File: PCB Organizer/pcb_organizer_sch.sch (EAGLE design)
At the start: 2 parts, among them U1 ARDUINO_NANO

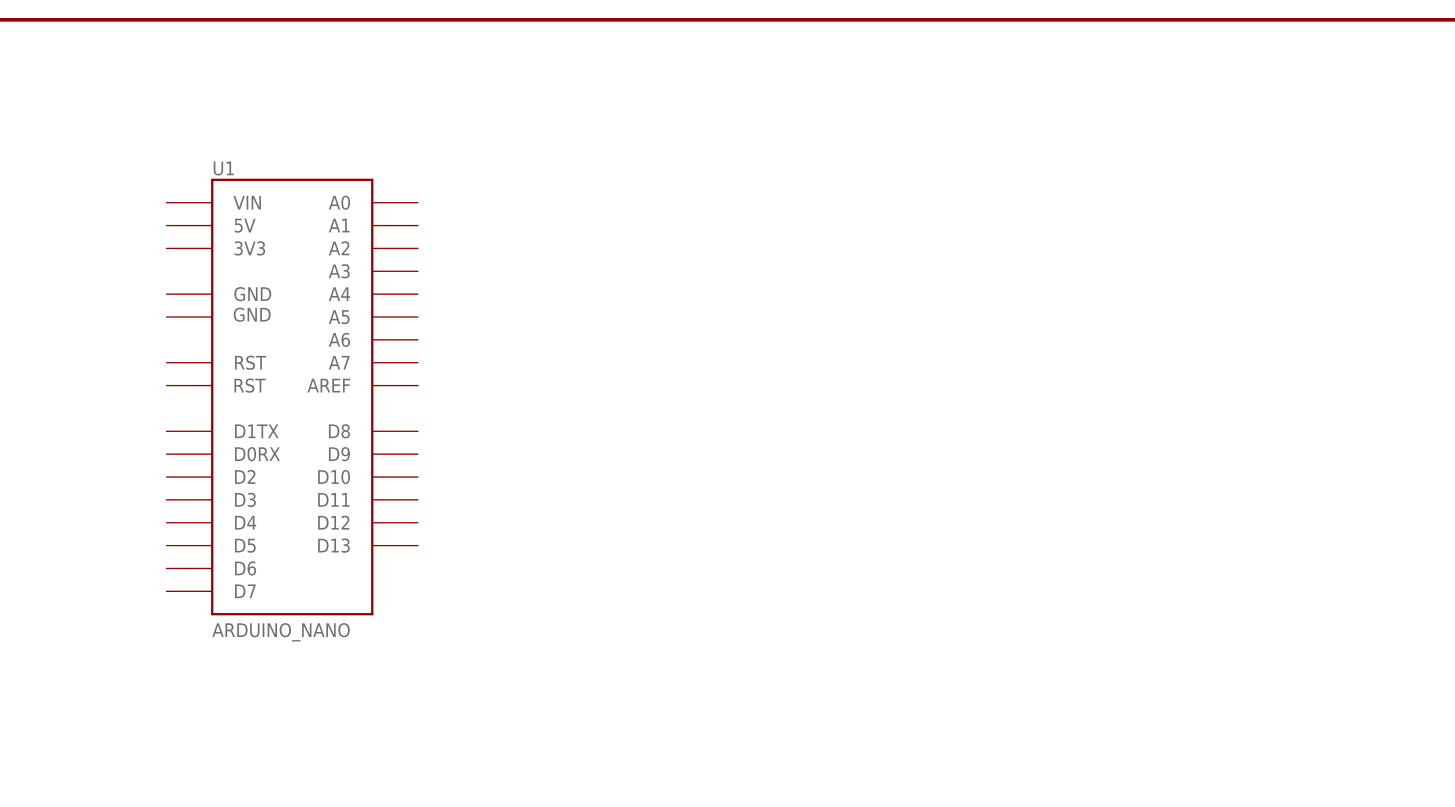
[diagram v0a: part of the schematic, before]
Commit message: Added footprint for V8FR-II receiver
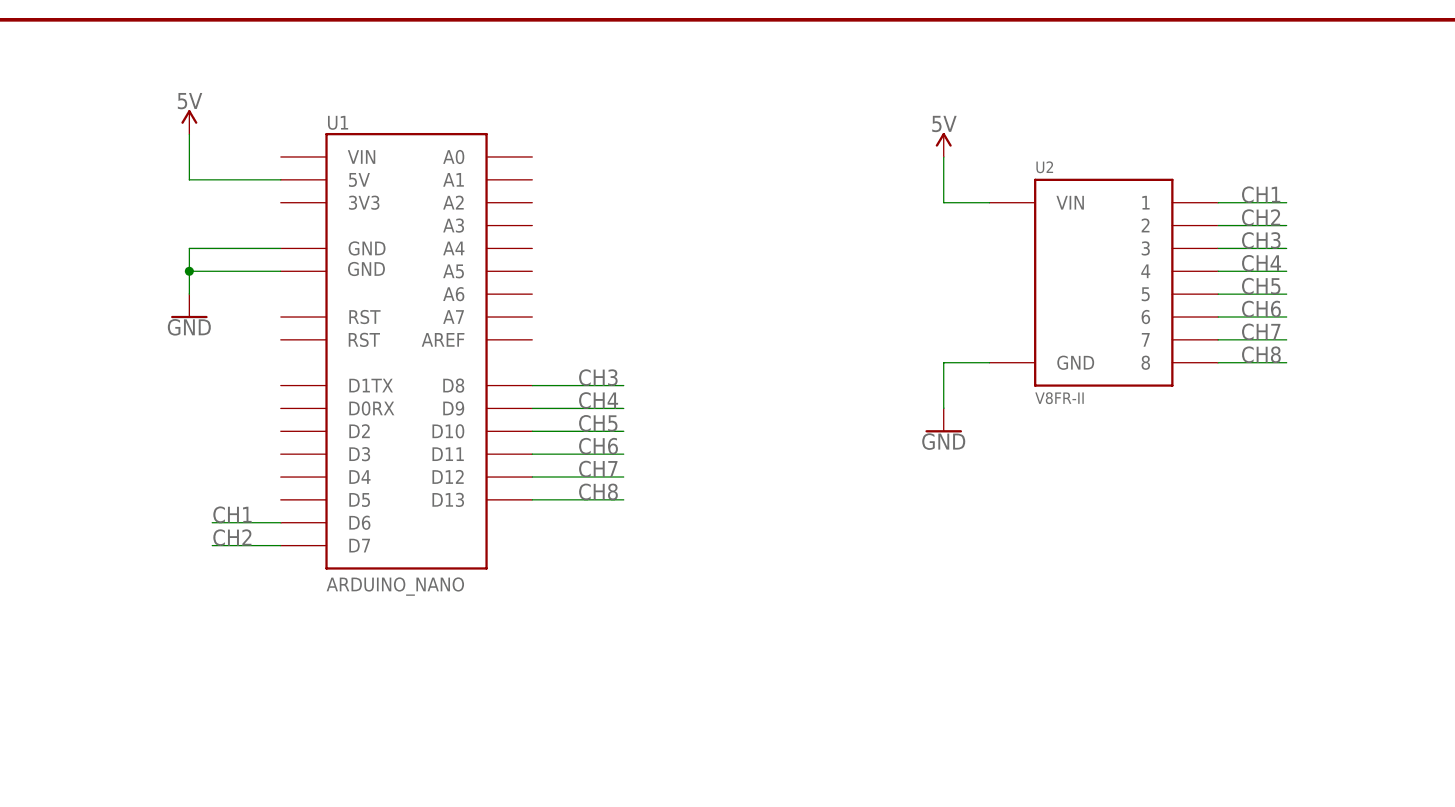
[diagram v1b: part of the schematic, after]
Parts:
- added U2: V8FR-II, CUCombatBots:V8FR-II
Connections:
- new net 5V: U1.5V, U2.VIN
- new net CH1: U1.D6, U2.1
- new net CH2: U1.D7, U2.2
- new net CH3: U1.D8, U2.3
- new net CH4: U1.D9, U2.4
- new net CH5: U1.D10, U2.5
- new net CH6: U1.D11, U2.6
- new net CH7: U1.D12, U2.7
- new net CH8: U1.D13, U2.8
- new net GND: U1.GND, U1.GND@16, U2.GND
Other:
- moved on the sheet: U1
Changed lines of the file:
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@@
 <part name="FRAME1" library="SparkFun-Aesthetics" deviceset="FRAME-LEDGER" device=""/>
 <part name="U1" library="CUCombatBots" deviceset="ARDUINO_NANO" device=""/>
+<part name="U2" library="CUCombatBots" deviceset="V8FR-II" device=""/>
+<part name="GND1" library="SparkFun-PowerSymbols" deviceset="GND" device=""/>
+<part name="GND2" library="SparkFun-PowerSymbols" deviceset="GND" device=""/>
+<part name="SUPPLY1" library="SparkFun-PowerSymbols" deviceset="5V" device=""/>
+<part name="SUPPLY2" library="SparkFun-PowerSymbols" deviceset="5V" device=""/>
 </parts>
 <sheets>
@@
 <attribute name="REV" x="419.1" y="6.604" size="2.7432" layer="94" font="vector"/>
 </instance>
-<instance part="U1" gate="G$1" x="60.96" y="246.38" smashed="yes">
-<attribute name="NAME" x="50.8" y="262.128" size="1.524" layer="95"/>
-<attribute name="VALUE" x="50.8" y="210.82" size="1.524" layer="96"/>
+<instance part="U1" gate="G$1" x="73.66" y="251.46" smashed="yes">
+<attribute name="NAME" x="63.5" y="267.208" size="1.524" layer="95"/>
+<attribute name="VALUE" x="63.5" y="215.9" size="1.524" layer="96"/>
+</instance>
+<instance part="U2" gate="G$1" x="149.86" y="251.46" smashed="yes">
+<attribute name="NAME" x="142.24" y="262.382" size="1.27" layer="95"/>
+<attribute name="VALUE" x="142.24" y="236.728" size="1.27" layer="96"/>
+</instance>
+<instance part="GND1" gate="1" x="132.08" y="233.68" smashed="yes">
+<attribute name="VALUE" x="132.08" y="233.426" size="1.778" layer="96" align="top-center"/>
+</instance>
+<instance part="GND2" gate="1" x="48.26" y="246.38" smashed="yes">
+<attribute name="VALUE" x="48.26" y="246.126" size="1.778" layer="96" align="top-center"/>
+</instance>
+<instance part="SUPPLY1" gate="G$1" x="48.26" y="266.7" smashed="yes">
+<attribute name="VALUE" x="48.26" y="269.494" size="1.778" layer="96" align="bottom-center"/>
+</instance>
+<instance part="SUPPLY2" gate="G$1" x="132.08" y="264.16" smashed="yes">
+<attribute name="VALUE" x="132.08" y="266.954" size="1.778" layer="96" align="bottom-center"/>
 </instance>
 </instances>
@@
 </busses>
 <nets>
+<net name="5V" class="0">
+<segment>
+<pinref part="U2" gate="G$1" pin="VIN"/>
+<wire x1="137.16" y1="259.08" x2="132.08" y2="259.08" width="0.1524" layer="91"/>
+<pinref part="SUPPLY2" gate="G$1" pin="5V"/>
+<wire x1="132.08" y1="259.08" x2="132.08" y2="264.16" width="0.1524" layer="91"/>
+</segment>
+<segment>
+<pinref part="U1" gate="G$1" pin="5V"/>
+<wire x1="58.42" y1="261.62" x2="48.26" y2="261.62" width="0.1524" layer="91"/>
+<pinref part="SUPPLY1" gate="G$1" pin="5V"/>
+<wire x1="48.26" y1="261.62" x2="48.26" y2="266.7" width="0.1524" layer="91"/>
+</segment>
+</net>
+<net name="CH1" class="0">
+<segment>
+<pinref part="U2" gate="G$1" pin="1"/>
+<wire x1="162.56" y1="259.08" x2="170.18" y2="259.08" width="0.1524" layer="91"/>
+<label x="165.1" y="259.08" size="1.778" layer="95"/>
+</segment>
+<segment>
+<pinref part="U1" gate="G$1" pin="D6"/>
+<wire x1="58.42" y1="223.52" x2="50.8" y2="223.52" width="0.1524" layer="91"/>
+<label x="50.8" y="223.52" size="1.778" layer="95"/>
+</segment>
+</net>
+<net name="CH2" class="0">
+<segment>
+<pinref part="U2" gate="G$1" pin="2"/>
+<wire x1="162.56" y1="256.54" x2="170.18" y2="256.54" width="0.1524" layer="91"/>
+<label x="165.1" y="256.54" size="1.778" layer="95"/>
+</segment>
+<segment>
+<pinref part="U1" gate="G$1" pin="D7"/>
+<wire x1="58.42" y1="220.98" x2="50.8" y2="220.98" width="0.1524" layer="91"/>
+<label x="50.8" y="220.98" size="1.778" layer="95"/>
+</segment>
+</net>
+<net name="CH3" class="0">
+<segment>
+<pinref part="U2" gate="G$1" pin="3"/>
+<wire x1="162.56" y1="254" x2="170.18" y2="254" width="0.1524" layer="91"/>
+<label x="165.1" y="254" size="1.778" layer="95"/>
+</segment>
+<segment>
+<pinref part="U1" gate="G$1" pin="D8"/>
+<wire x1="86.36" y1="238.76" x2="96.52" y2="238.76" width="0.1524" layer="91"/>
+<label x="91.44" y="238.76" size="1.778" layer="95"/>
+</segment>
+</net>
+<net name="CH4" class="0">
+<segment>
+<pinref part="U2" gate="G$1" pin="4"/>
+<wire x1="162.56" y1="251.46" x2="170.18" y2="251.46" width="0.1524" layer="91"/>
+<label x="165.1" y="251.46" size="1.778" layer="95"/>
+</segment>
+<segment>
+<pinref part="U1" gate="G$1" pin="D9"/>
+<wire x1="86.36" y1="236.22" x2="96.52" y2="236.22" width="0.1524" layer="91"/>
+<label x="91.44" y="236.22" size="1.778" layer="95"/>
+</segment>
+</net>
+<net name="CH5" class="0">
+<segment>
+<pinref part="U2" gate="G$1" pin="5"/>
+<wire x1="162.56" y1="248.92" x2="170.18" y2="248.92" width="0.1524" layer="91"/>
+<label x="165.1" y="248.92" size="1.778" layer="95"/>
+</segment>
+<segment>
+<pinref part="U1" gate="G$1" pin="D10"/>
+<wire x1="86.36" y1="233.68" x2="96.52" y2="233.68" width="0.1524" layer="91"/>
+<label x="91.44" y="233.68" size="1.778" layer="95"/>
+</segment>
+</net>
+<net name="CH6" class="0">
+<segment>
+<pinref part="U2" gate="G$1" pin="6"/>
+<wire x1="162.56" y1="246.38" x2="170.18" y2="246.38" width="0.1524" layer="91"/>
+<label x="165.1" y="246.38" size="1.778" layer="95"/>
+</segment>
+<segment>
+<pinref part="U1" gate="G$1" pin="D11"/>
+<wire x1="86.36" y1="231.14" x2="96.52" y2="231.14" width="0.1524" layer="91"/>
+<label x="91.44" y="231.14" size="1.778" layer="95"/>
+</segment>
+</net>
+<net name="CH7" class="0">
+<segment>
+<pinref part="U2" gate="G$1" pin="7"/>
+<wire x1="162.56" y1="243.84" x2="170.18" y2="243.84" width="0.1524" layer="91"/>
+<label x="165.1" y="243.84" size="1.778" layer="95"/>
+</segment>
+<segment>
+<pinref part="U1" gate="G$1" pin="D12"/>
+<wire x1="86.36" y1="228.6" x2="96.52" y2="228.6" width="0.1524" layer="91"/>
+<label x="91.44" y="228.6" size="1.778" layer="95"/>
+</segment>
+</net>
+<net name="CH8" class="0">
+<segment>
+<pinref part="U2" gate="G$1" pin="8"/>
+<wire x1="162.56" y1="241.3" x2="170.18" y2="241.3" width="0.1524" layer="91"/>
+<label x="165.1" y="241.3" size="1.778" layer="95"/>
+</segment>
+<segment>
+<pinref part="U1" gate="G$1" pin="D13"/>
+<wire x1="86.36" y1="226.06" x2="96.52" y2="226.06" width="0.1524" layer="91"/>
+<label x="91.44" y="226.06" size="1.778" layer="95"/>
+</segment>
+</net>
+<net name="GND" class="0">
+<segment>
+<pinref part="U2" gate="G$1" pin="GND"/>
+<wire x1="137.16" y1="241.3" x2="132.08" y2="241.3" width="0.1524" layer="91"/>
+<pinref part="GND1" gate="1" pin="GND"/>
+<wire x1="132.08" y1="236.22" x2="132.08" y2="241.3" width="0.1524" layer="91"/>
+</segment>
+<segment>
+<pinref part="U1" gate="G$1" pin="GND"/>
+<wire x1="58.42" y1="254" x2="48.26" y2="254" width="0.1524" layer="91"/>
+<wire x1="48.26" y1="254" x2="48.26" y2="251.46" width="0.1524" layer="91"/>
+<pinref part="U1" gate="G$1" pin="GND@16"/>
+<wire x1="48.26" y1="251.46" x2="58.42" y2="251.46" width="0.1524" layer="91"/>
+<wire x1="48.26" y1="251.46" x2="48.26" y2="248.92" width="0.1524" layer="91"/>
+<junction x="48.26" y="251.46"/>
+<pinref part="GND2" gate="1" pin="GND"/>
+</segment>
+</net>
 </nets>
 </sheet>

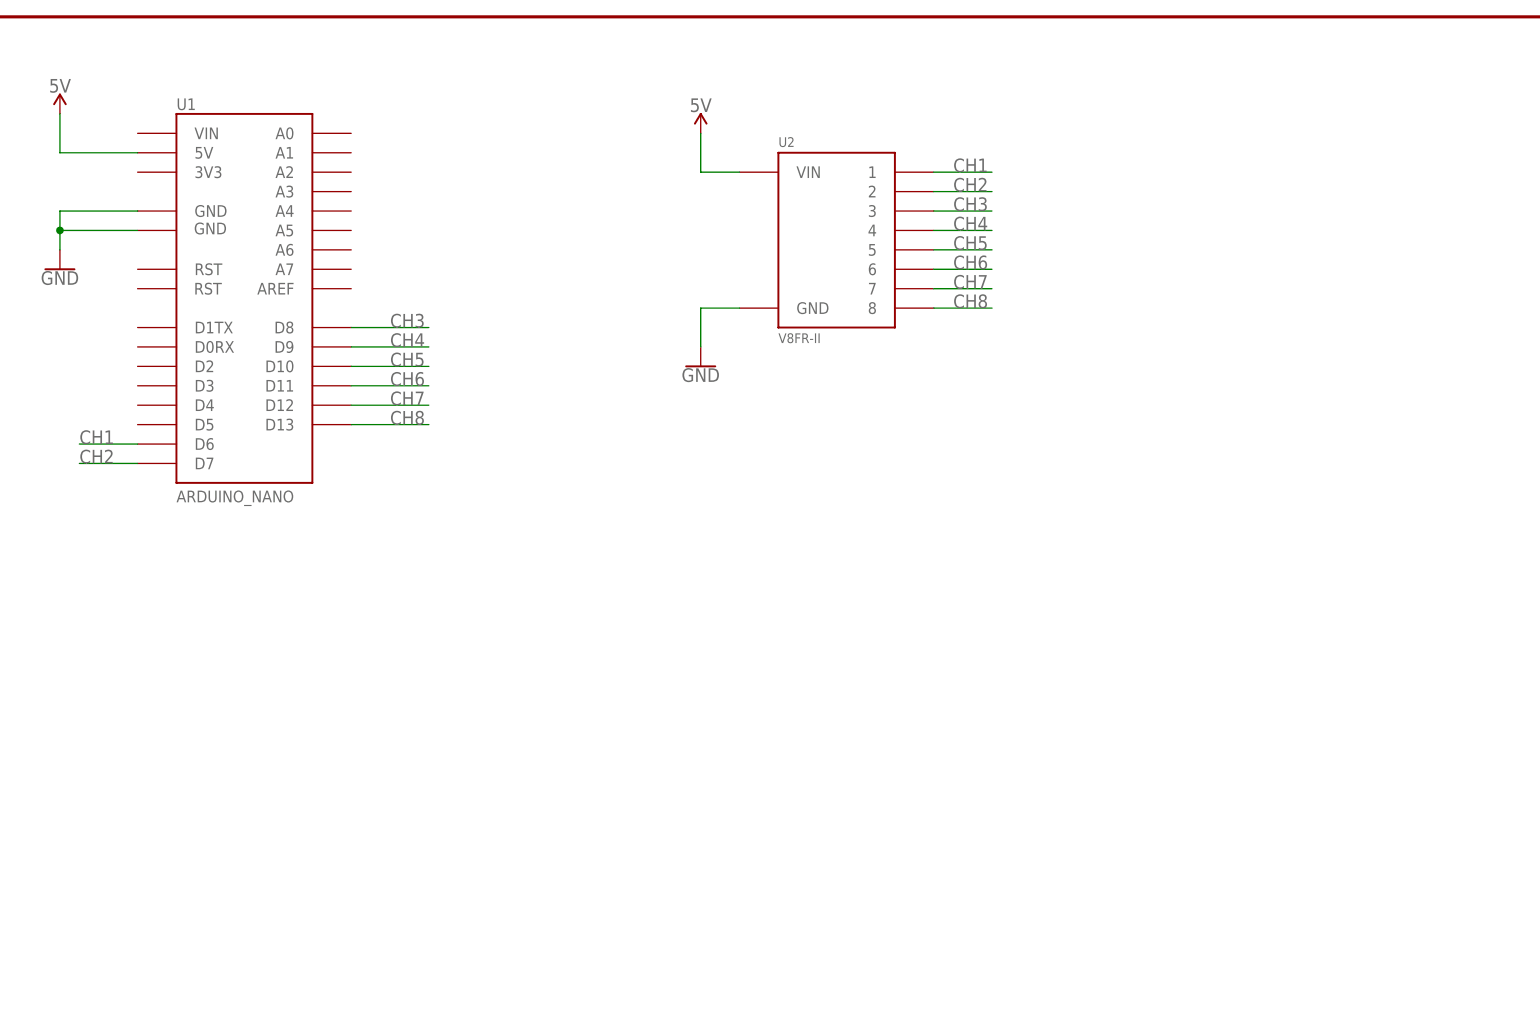
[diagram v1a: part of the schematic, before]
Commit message: Added Pololu TB67 motor driver to the library, board, and schematic
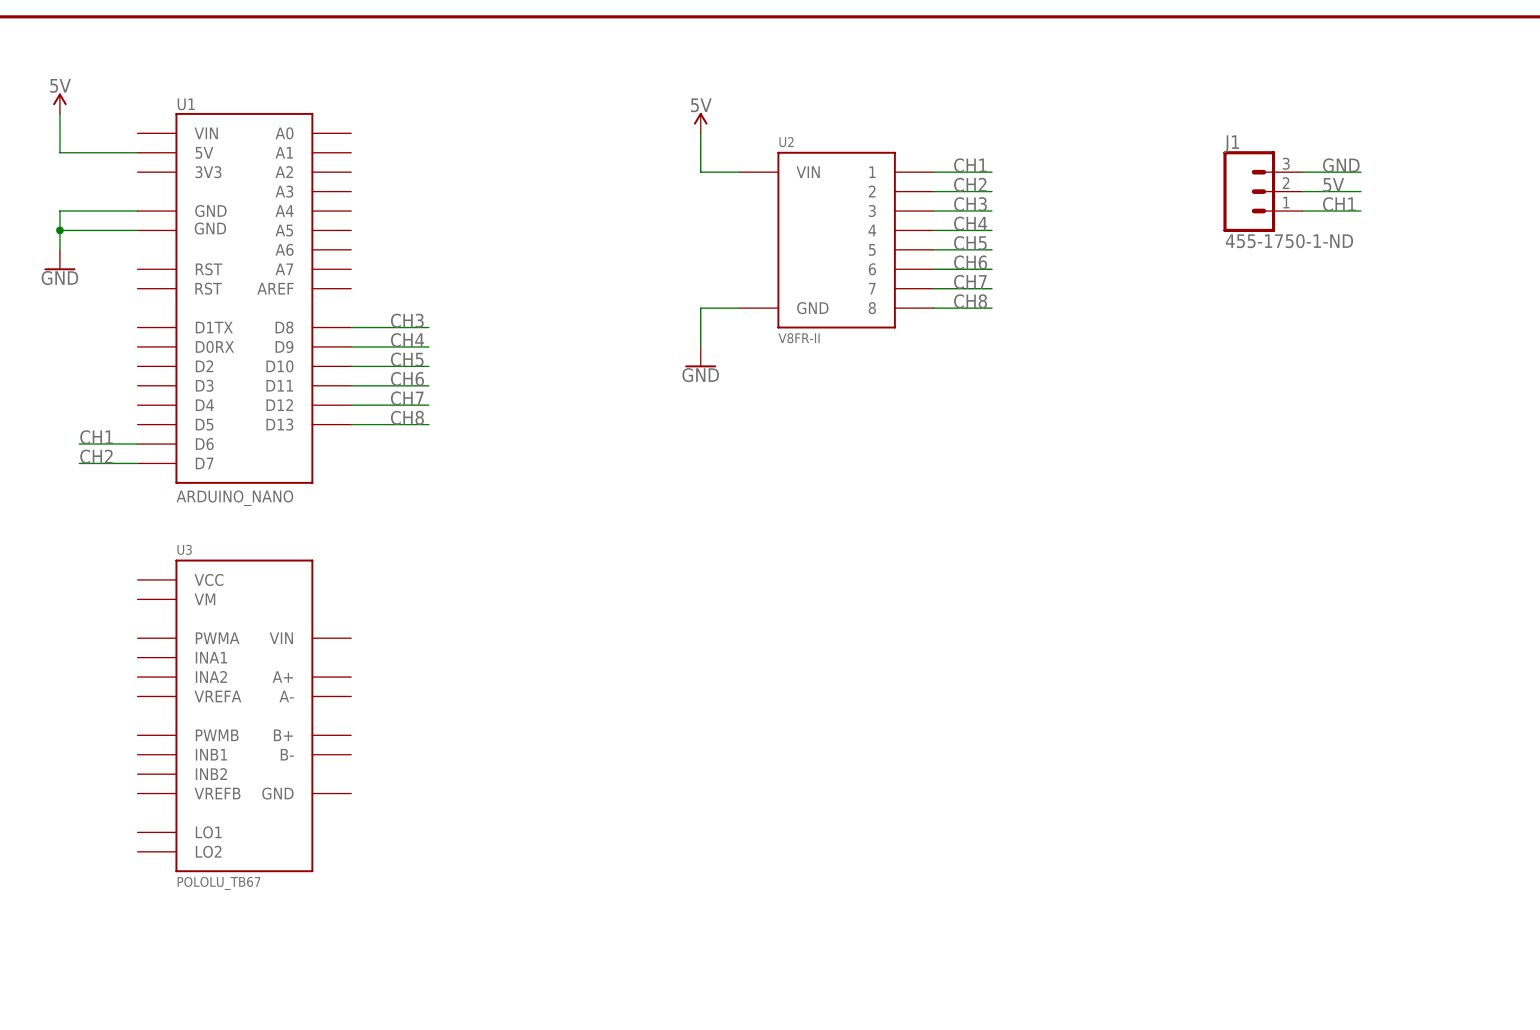
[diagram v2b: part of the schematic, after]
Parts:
- added J1: 455-1750-1-ND, SparkFun-Connectors:CONN_03
- added U3: POLOLU_TB67, CUCombatBots:POLOLU_TB67
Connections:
- net 5V: now also J1.2
- net CH1: now also J1.1
- net GND: now also J1.3
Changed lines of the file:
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@@
 <part name="SUPPLY1" library="SparkFun-PowerSymbols" deviceset="5V" device=""/>
 <part name="SUPPLY2" library="SparkFun-PowerSymbols" deviceset="5V" device=""/>
+<part name="J1" library="SparkFun-Connectors" deviceset="CONN_03" device="" value="455-1750-1-ND"/>
+<part name="U3" library="CUCombatBots" deviceset="POLOLU_TB67" device=""/>
 </parts>
 <sheets>
@@
 <attribute name="VALUE" x="132.08" y="266.954" size="1.778" layer="96" align="bottom-center"/>
 </instance>
+<instance part="J1" gate="J$1" x="203.2" y="256.54" smashed="yes">
+<attribute name="VALUE" x="200.66" y="249.174" size="1.778" layer="96" font="vector"/>
+<attribute name="NAME" x="200.66" y="262.128" size="1.778" layer="95" font="vector"/>
+</instance>
+<instance part="U3" gate="G$1" x="73.66" y="193.04" smashed="yes">
+<attribute name="NAME" x="63.5" y="209.042" size="1.27" layer="95"/>
+<attribute name="VALUE" x="63.5" y="165.608" size="1.27" layer="96"/>
+</instance>
 </instances>
 <busses>
@@
 <wire x1="48.26" y1="261.62" x2="48.26" y2="266.7" width="0.1524" layer="91"/>
 </segment>
+<segment>
+<pinref part="J1" gate="J$1" pin="2"/>
+<wire x1="210.82" y1="256.54" x2="218.44" y2="256.54" width="0.1524" layer="91"/>
+<label x="213.36" y="256.54" size="1.778" layer="95"/>
+</segment>
 </net>
 <net name="CH1" class="0">
@@
 <wire x1="58.42" y1="223.52" x2="50.8" y2="223.52" width="0.1524" layer="91"/>
 <label x="50.8" y="223.52" size="1.778" layer="95"/>
+</segment>
+<segment>
+<pinref part="J1" gate="J$1" pin="1"/>
+<wire x1="210.82" y1="254" x2="218.44" y2="254" width="0.1524" layer="91"/>
+<label x="213.36" y="254" size="1.778" layer="95"/>
 </segment>
 </net>
@@
 <pinref part="GND2" gate="1" pin="GND"/>
 </segment>
+<segment>
+<pinref part="J1" gate="J$1" pin="3"/>
+<wire x1="210.82" y1="259.08" x2="218.44" y2="259.08" width="0.1524" layer="91"/>
+<label x="213.36" y="259.08" size="1.778" layer="95"/>
+</segment>
 </net>
